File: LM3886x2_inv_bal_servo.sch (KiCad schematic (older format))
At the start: 66 parts, among them J1 INPUT, J2 OUT, J3 36V, J4 15V, U1 NE5532, U2 NE5532, U3 OPA2134, U4 LM3886, U5 LM3886

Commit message: updated sch
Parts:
- removed R3, R4: 1K, symbol Device:R_Small
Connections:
- net GND: now also C13.2, C14.1, R5.2
- net at C14.2, R2.1: now also C16.2
- net at C13.1, R1.1: now also C15.2
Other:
- note added: "JFET input opamp"
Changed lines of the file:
@@
-$EndComp
-$Comp
-L Device:R_Small R3
-U 1 1 64A1AA11
-P 1650 3000
-F 0 "R3" V 1454 3000 50  0000 C CNN
-F 1 "1K" V 1545 3000 50  0000 C CNN
-F 2 "" H 1650 3000 50  0001 C CNN
-F 3 "~" H 1650 3000 50  0001 C CNN
-	1    1650 3000
-	0    1    1    0
 $EndComp
 $Comp
@@
 $EndComp
 $Comp
-L Device:R_Small R4
-U 1 1 64A1C54A
-P 1650 4000
-F 0 "R4" V 1454 4000 50  0000 C CNN
-F 1 "1K" V 1545 4000 50  0000 C CNN
-F 2 "" H 1650 4000 50  0001 C CNN
-F 3 "~" H 1650 4000 50  0001 C CNN
-	1    1650 4000
-	0    1    1    0
-$EndComp
-$Comp
 L power:GND #PWR01
 U 1 1 64A1FC29
@@
 Connection ~ 1500 3000
 Wire Wire Line
-	1500 3000 1550 3000
-Wire Wire Line
 	1500 3300 1500 3450
 Wire Wire Line
@@
 	1500 3700 1500 4000
 Connection ~ 1500 4000
-Wire Wire Line
-	1500 4000 1550 4000
 $Comp
 L Device:C_Small C15
@@
 	2200 3450 2200 3550
 Wire Wire Line
-	1750 3000 1900 3000
-Wire Wire Line
 	2200 3100 2200 3000
 Wire Wire Line
@@
 Wire Wire Line
 	2200 4000 2100 4000
-Wire Wire Line
-	1900 4000 1750 4000
 $Comp
 L Device:R_Small R8
@@
 	9750 3000 10150 3000
 Connection ~ 9750 3000
+Wire Wire Line
+	1500 3000 1900 3000
+Wire Wire Line
+	1500 4000 1900 4000
+$Comp
+L power:GND #PWR?
+U 1 1 64EE1A26
+P 1300 3500
+F 0 "#PWR?" H 1300 3250 50  0001 C CNN
+F 1 "GND" H 1305 3327 50  0001 C CNN
+F 2 "" H 1300 3500 50  0001 C CNN
+F 3 "" H 1300 3500 50  0001 C CNN
+	1    1300 3500
+	1    0    0    -1
+$EndComp
+Wire Wire Line
+	1300 3500 1300 3450
+Wire Wire Line
+	1300 3450 1500 3450
+Text Notes 7550 1450 0    50   ~ 0
+JFET input opamp
+Text Notes 7550 4250 0    50   ~ 0
+JFET input opamp
 $EndSCHEMATC

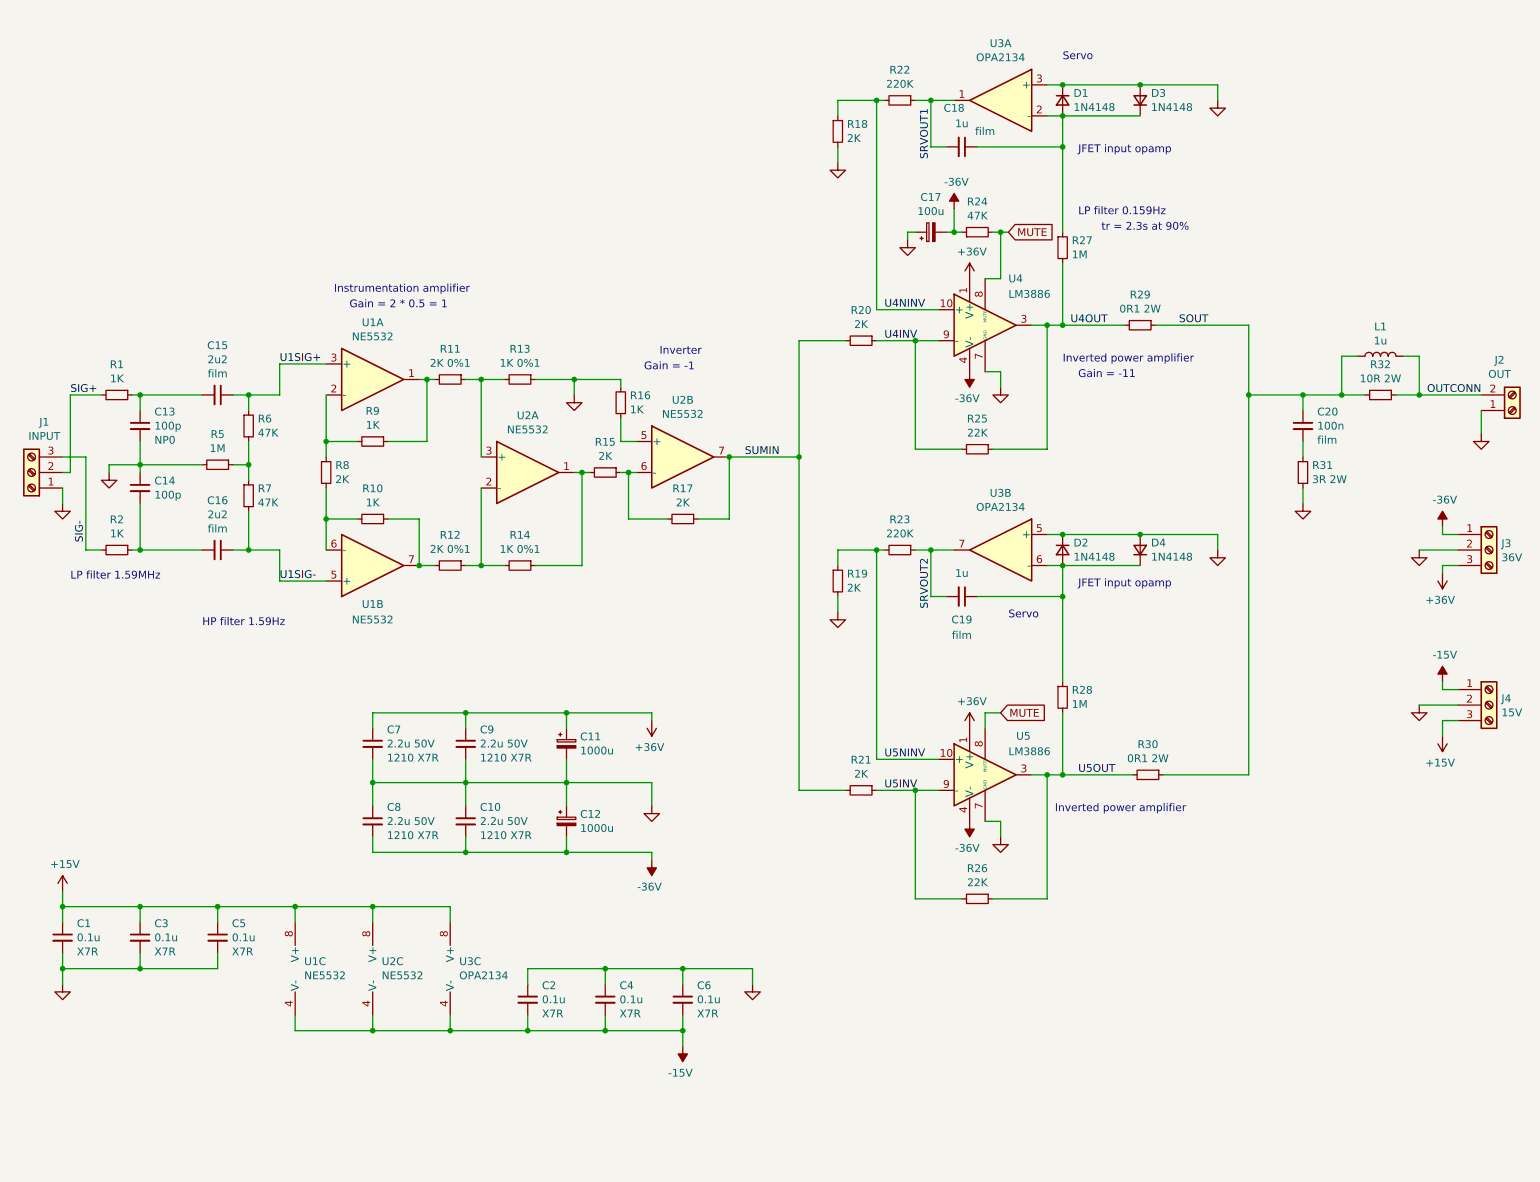
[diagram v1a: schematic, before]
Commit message: pcb is started
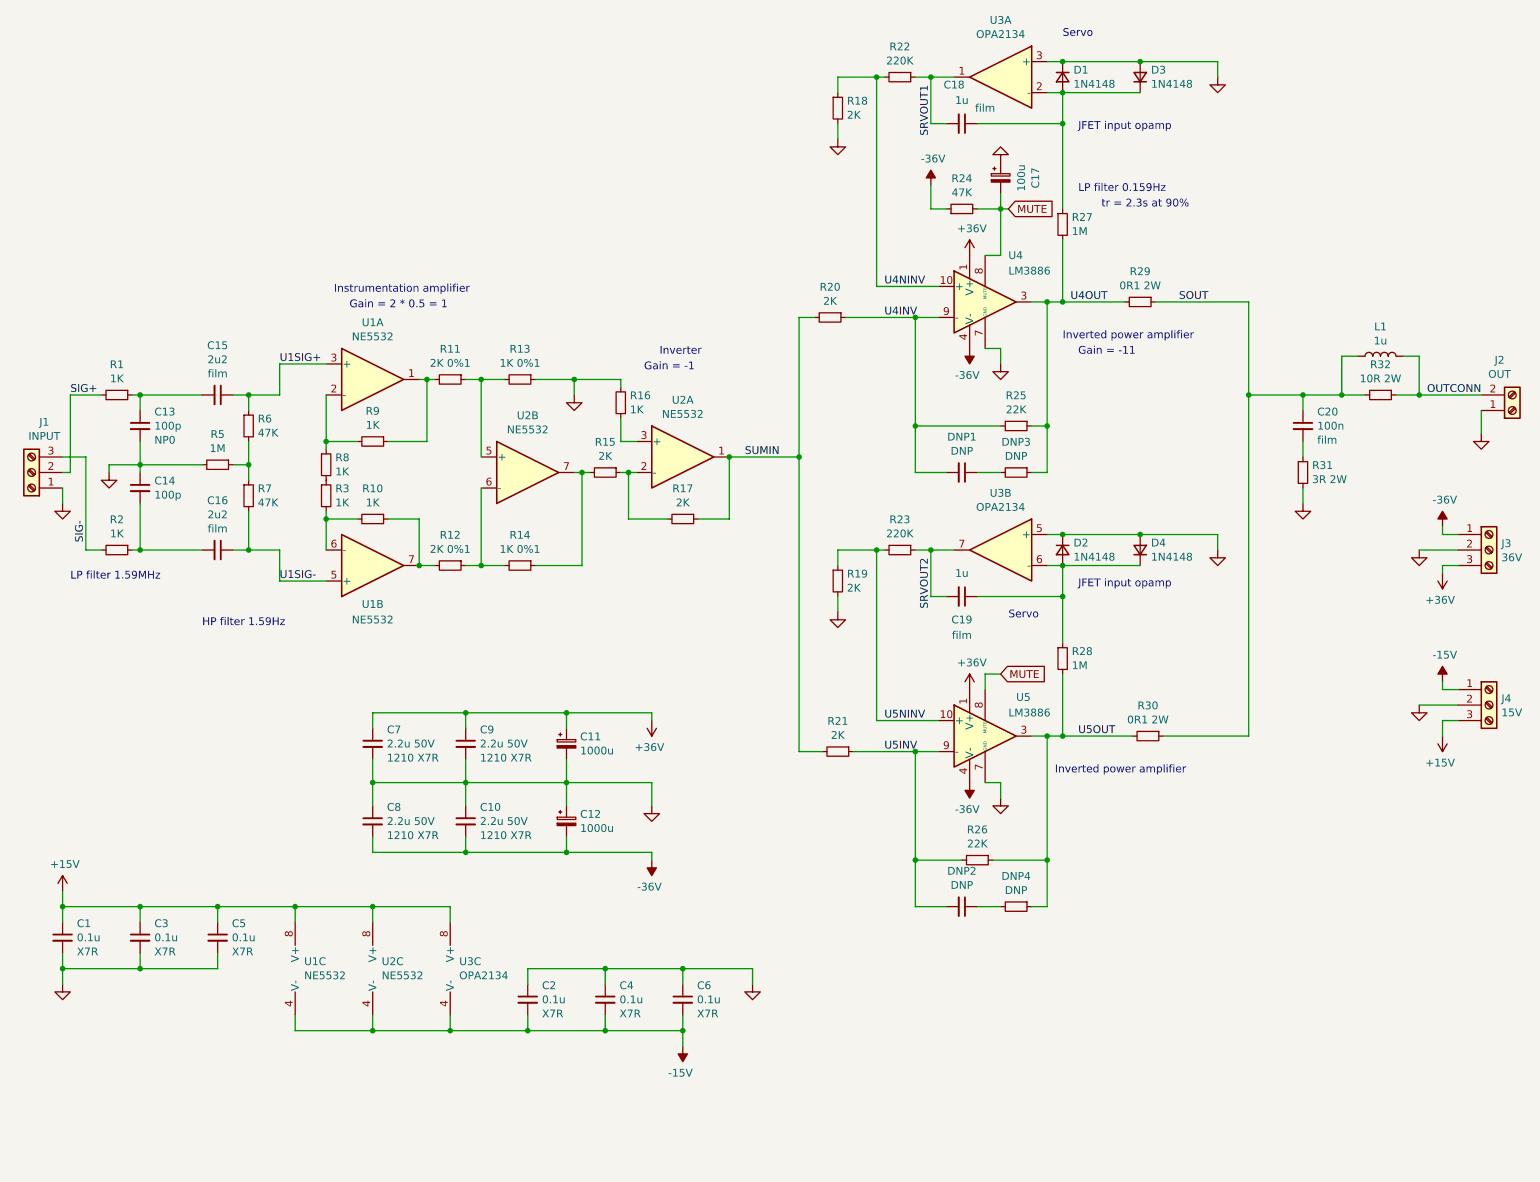
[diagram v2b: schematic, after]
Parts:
- added DNP1, DNP2: DNP, Capacitor_SMD:C_0805_2012Metric_Pad1.15x1.40mm_HandSolder, symbol Device:C_Small
- added DNP3, DNP4: DNP, Resistor_SMD:R_1206_3216Metric_Pad1.42x1.75mm_HandSolder, symbol Device:R_Small
- added R3: 1K, Resistor_SMD:R_1206_3216Metric_Pad1.42x1.75mm_HandSolder, symbol Device:R_Small
- C1, C13, C14, C2, C3, C4, C5, C6: footprint (none) -> Capacitor_SMD:C_1206_3216Metric_Pad1.42x1.75mm_HandSolder
- C10, C7, C8, C9: footprint (none) -> Capacitor_SMD:C_1210_3225Metric_Pad1.42x2.65mm_HandSolder
- C11, C12: footprint (none) -> Capacitor_THT:CP_Radial_D16.0mm_P7.50mm
- C15, C16, C18, C19: footprint (none) -> Capacitor_THT:C_Rect_L7.2mm_W5.5mm_P5.00mm_FKS2_FKP2_MKS2_MKP2
- C17: footprint (none) -> Capacitor_THT:CP_Radial_D8.0mm_P3.80mm
- C20: footprint (none) -> Capacitor_THT:C_Rect_L7.2mm_W2.5mm_P5.00mm_FKS2_FKP2_MKS2_MKP2
- D1, D2, D3, D4: footprint (none) -> Diode_SMD:D_SOD-123
- J1, J4: footprint (none) -> local_footprints_lib:TerminalBlock_ Amphenol_01_03_P3.50mm
- J2: footprint (none) -> local_footprints_lib:TerminalBlock_CUI_01x02_P5.00mm
- J3: footprint (none) -> local_footprints_lib:TerminalBlock_CUI_01x03_P5.00mm
- L1: footprint (none) -> local_footprints_lib:Inductor_DIY
- R1, R10, R11, R12, R13, R14, R15, R16, R17, R18, R19, R2, R20, R21, R22, R23, R24, R25, R26, R27, R28, R5, R6, R7, R9: footprint (none) -> Resistor_SMD:R_1206_3216Metric_Pad1.42x1.75mm_HandSolder
- R29, R30, R31, R32: footprint (none) -> Resistor_SMD:R_2512_6332Metric_Pad1.52x3.35mm_HandSolder
- R8: value 2K -> 1K; footprint (none) -> Resistor_SMD:R_1206_3216Metric_Pad1.42x1.75mm_HandSolder
- U1, U2, U3: footprint (none) -> Package_SO:SOIC-8_3.9x4.9mm_P1.27mm
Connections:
- net -36V: no longer C17.2
- net MUTE: now also C17.2
- net SUMIN: now also U2.1; no longer U2.7
- net U4INV: now also DNP1.2
- net U4OUT: now also DNP3.1
- net U5INV: now also DNP2.2
- net U5OUT: now also DNP4.1
- net at R10.2, U1.6 (-): now also R3.2; no longer R8.2
- net at R14.1, R15.2: now also U2.7; no longer U2.1
- net at R12.1, R14.2: now also U2.6 (-); no longer U2.2 (-)
- net at R11.1, R13.2: now also U2.5 (+); no longer U2.3 (+)
- net at R16.1: now also U2.3 (+); no longer U2.5 (+)
- net at R15.1, R17.2: now also U2.2 (-); no longer U2.6 (-)
- new net: DNP1.1, DNP3.2
- new net: R3.1, R8.2
- new net: DNP2.1, DNP4.2
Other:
- moved on the sheet: C17, C18, D1, D3, R18, R20, R21, R22, R24, R25, R26, R27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

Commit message: finished PCB layout
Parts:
- added H1, H2, H3, H4: MountingHole, MountingHole:MountingHole_3.2mm_M3_Pad_Via, symbol Mechanical:MountingHole
- R5: value 1M -> 2M2
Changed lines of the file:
@@
 P 2000 3450
 F 0 "R5" V 1804 3450 50  0000 C CNN
-F 1 "1M" V 1895 3450 50  0000 C CNN
+F 1 "2M2" V 1895 3450 50  0000 C CNN
 F 2 "Resistor_SMD:R_1206_3216Metric_Pad1.42x1.75mm_HandSolder" H 2000 3450 50  0001 C CNN
 F 3 "~" H 2000 3450 50  0001 C CNN
@@
 U 1 1 64A800A8
 P 7050 1600
-F 0 "C17" V 7275 1600 50  0000 C CNN
-F 1 "100u" V 7184 1600 50  0000 C CNN
+F 0 "C17" H 7250 1700 50  0000 C CNN
+F 1 "100u" H 7250 1600 50  0000 C CNN
 F 2 "Capacitor_THT:CP_Radial_D8.0mm_P3.80mm" H 7050 1600 50  0001 C CNN
 F 3 "~" H 7050 1600 50  0001 C CNN
@@
 Wire Wire Line
 	6600 1800 6600 1650
+$Comp
+L Mechanical:MountingHole H3
+U 1 1 64A55F61
+P 750 7700
+F 0 "H3" H 850 7746 50  0000 L CNN
+F 1 "MountingHole" H 850 7655 50  0000 L CNN
+F 2 "MountingHole:MountingHole_3.2mm_M3_Pad_Via" H 750 7700 50  0001 C CNN
+F 3 "~" H 750 7700 50  0001 C CNN
+	1    750  7700
+	1    0    0    -1
+$EndComp
+$Comp
+L Mechanical:MountingHole H4
+U 1 1 64A56BA7
+P 750 7900
+F 0 "H4" H 850 7946 50  0000 L CNN
+F 1 "MountingHole" H 850 7855 50  0000 L CNN
+F 2 "MountingHole:MountingHole_3.2mm_M3_Pad_Via" H 750 7900 50  0001 C CNN
+F 3 "~" H 750 7900 50  0001 C CNN
+	1    750  7900
+	1    0    0    -1
+$EndComp
+$Comp
+L Mechanical:MountingHole H2
+U 1 1 64A5762B
+P 750 7500
+F 0 "H2" H 850 7546 50  0000 L CNN
+F 1 "MountingHole" H 850 7455 50  0000 L CNN
+F 2 "MountingHole:MountingHole_3.2mm_M3_Pad_Via" H 750 7500 50  0001 C CNN
+F 3 "~" H 750 7500 50  0001 C CNN
+	1    750  7500
+	1    0    0    -1
+$EndComp
+$Comp
+L Mechanical:MountingHole H1
+U 1 1 64A57A93
+P 750 7300
+F 0 "H1" H 850 7346 50  0000 L CNN
+F 1 "MountingHole" H 850 7255 50  0000 L CNN
+F 2 "MountingHole:MountingHole_3.2mm_M3_Pad_Via" H 750 7300 50  0001 C CNN
+F 3 "~" H 750 7300 50  0001 C CNN
+	1    750  7300
+	1    0    0    -1
+$EndComp
 $EndSCHEMATC
